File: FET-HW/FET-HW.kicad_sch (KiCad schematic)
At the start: 12 parts

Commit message: Remember that I needed 3x FETS per leg
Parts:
- removed N? (x2): Pad_4x2, N_NonPart:Pad_4x2, symbol N_NonPart:Pad_4x2
- removed Q? (x6): IRF7769L1TRPBF, Q_MOSFET:IR_DirectFET_L8, symbol Q_MOSFET:IRF7769L1TRPBF
- added N4, N5: Pad_4x2, N_NonPart:Pad_4x2, symbol N_NonPart:Pad_4x2
- gave numbers to parts that had none: 4
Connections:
- net PHASE_B: now also N4.1
- net PHASE_C: now also N5.1
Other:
- added sheet Half-Bridge-A (Half-Bridge.kicad_sch)
- added sheet Half-Bridge-B (Half-Bridge.kicad_sch)
- added sheet Half-Bridge-C (Half-Bridge.kicad_sch)
- note removed: "BLCD Interface"
- moved on the sheet: N3

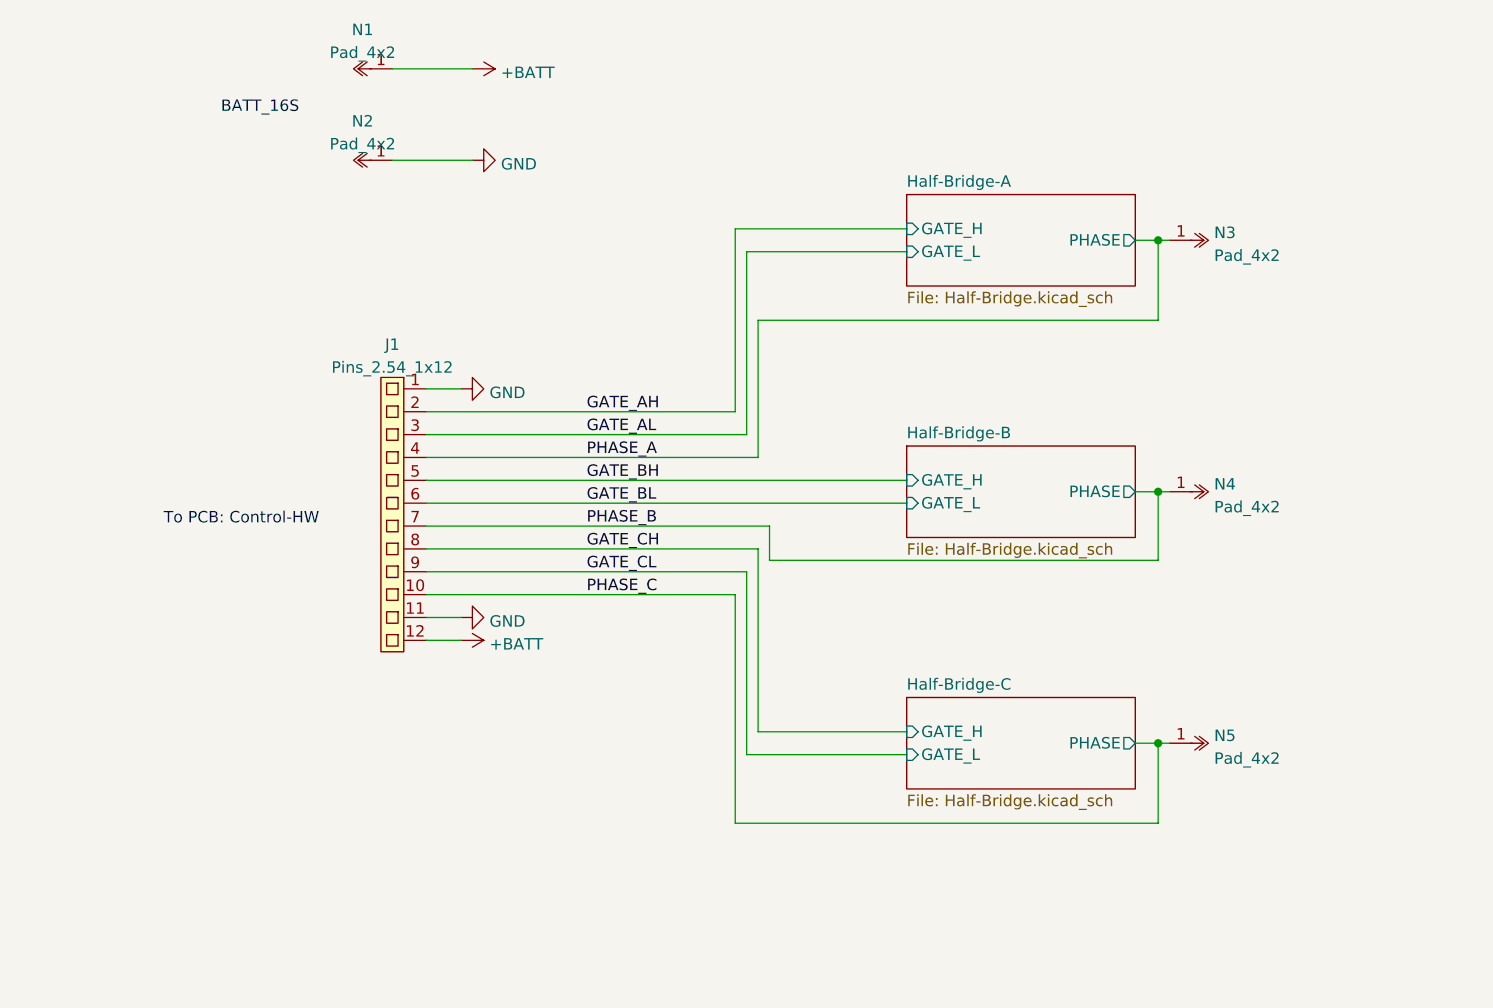
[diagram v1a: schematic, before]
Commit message: First pass at FET PCB layout
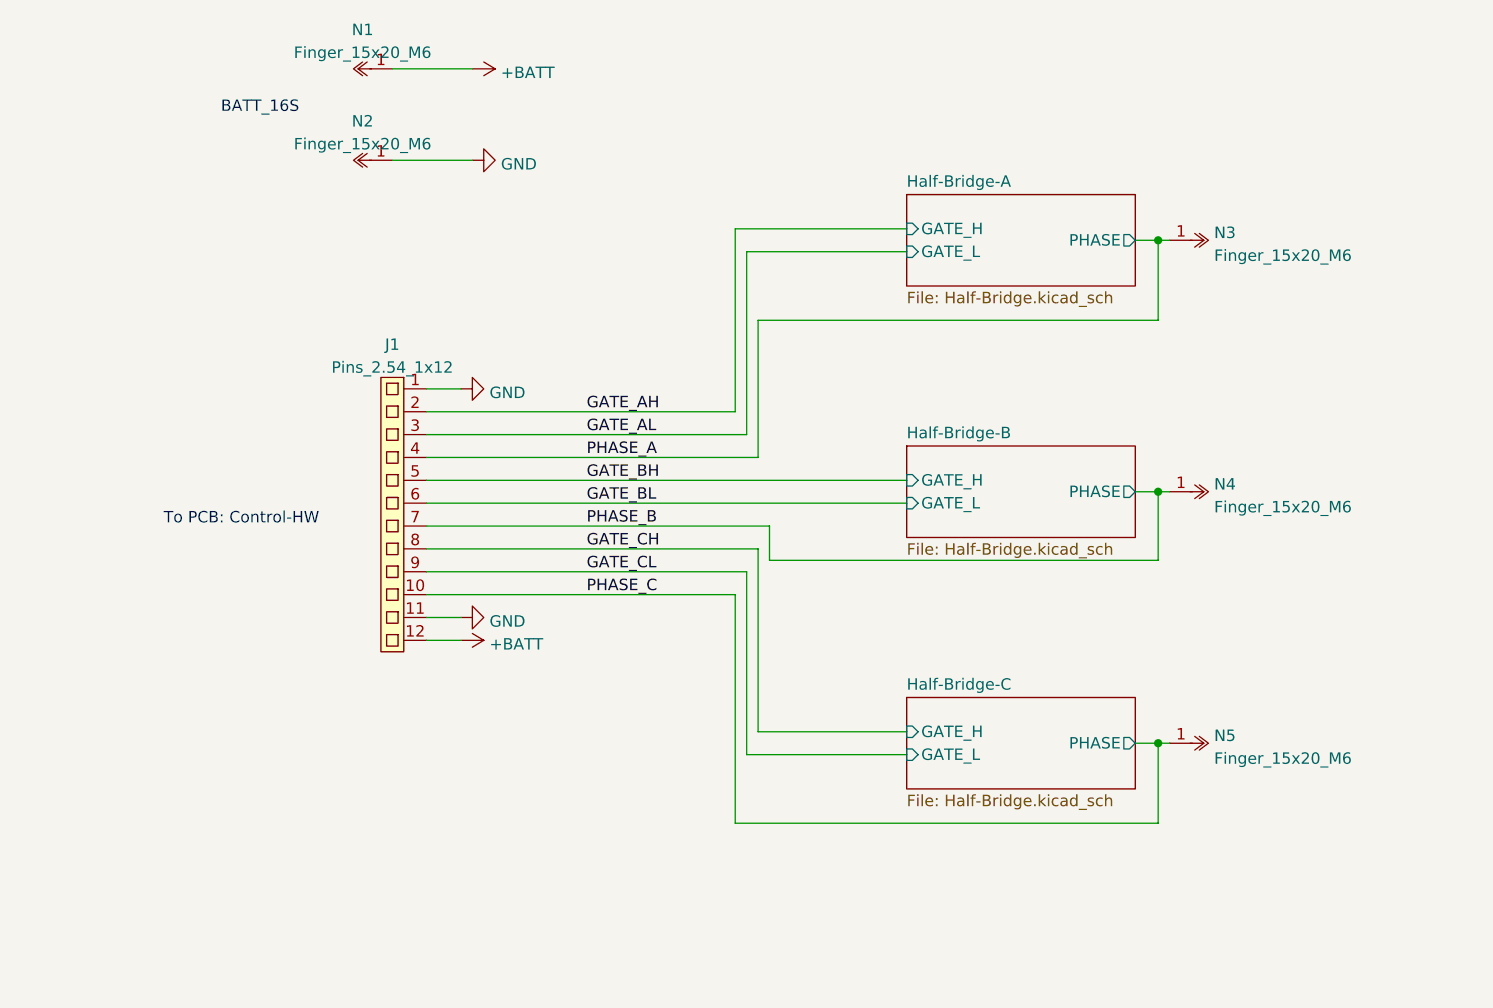
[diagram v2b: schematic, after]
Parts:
- removed N1, N2, N3, N4, N5: Pad_4x2, N_NonPart:Pad_4x2, symbol N_NonPart:Pad_4x2
- added N1, N2, N3, N4, N5: Finger_15x20_M6, N_NonPart:Finger_15x20_M6, symbol N_NonPart:Finger_15x20_M6
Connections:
- net +BATT: now also N1.1
- net GND: now also N2.1
- net PHASE_A: now also N3.1
- net PHASE_B: now also N4.1
- net PHASE_C: now also N5.1
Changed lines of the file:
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@@
     (pin "1")
   )
-  (symbol (lib_id "N_NonPart:Pad_4x2") (at 172.72 119.38 0) (unit 1)
+  (symbol (lib_id "N_NonPart:Finger_15x20_M6") (at 172.72 119.38 0) (unit 1)
     (in_bom no) (on_board yes) (fields_autoplaced)
     (property "Reference" "N5" (id 0) (at 176.403 118.5453 0)
       (effects (font (size 1.27 1.27)) (justify left))
     )
-    (property "Value" "Pad_4x2" (id 1) (at 176.403 121.0822 0)
-      (effects (font (size 1.27 1.27)) (justify left))
-    )
-    (property "Footprint" "N_NonPart:Pad_4x2" (id 2) (at 172.72 121.666 0)
+    (property "Value" "Finger_15x20_M6" (id 1) (at 176.403 121.0822 0)
+      (effects (font (size 1.27 1.27)) (justify left))
+    )
+    (property "Footprint" "N_NonPart:Finger_15x20_M6" (id 2) (at 172.72 121.666 0)
       (effects (font (size 1.27 1.27)) hide)
     )
     (property "Datasheet" "" (id 3) (at 172.72 121.666 0)
-      (effects (font (size 1.27 1.27)) hide)
-    )
-    (pin "1")
-  )
-  (symbol (lib_id "N_NonPart:Pad_4x2") (at 83.82 44.45 180) (unit 1)
-    (in_bom no) (on_board yes) (fields_autoplaced)
-    (property "Reference" "N1" (id 0) (at 81.788 40.1152 0))
-    (property "Value" "Pad_4x2" (id 1) (at 81.788 42.6521 0))
-    (property "Footprint" "N_NonPart:Pad_4x2" (id 2) (at 83.82 42.164 0)
-      (effects (font (size 1.27 1.27)) hide)
-    )
-    (property "Datasheet" "" (id 3) (at 83.82 42.164 0)
       (effects (font (size 1.27 1.27)) hide)
     )
@@
     (pin "9")
   )
-  (symbol (lib_id "N_NonPart:Pad_4x2") (at 172.72 91.44 0) (unit 1)
+  (symbol (lib_id "N_NonPart:Finger_15x20_M6") (at 172.72 91.44 0) (unit 1)
     (in_bom no) (on_board yes) (fields_autoplaced)
     (property "Reference" "N4" (id 0) (at 176.403 90.6053 0)
       (effects (font (size 1.27 1.27)) (justify left))
     )
-    (property "Value" "Pad_4x2" (id 1) (at 176.403 93.1422 0)
-      (effects (font (size 1.27 1.27)) (justify left))
-    )
-    (property "Footprint" "N_NonPart:Pad_4x2" (id 2) (at 172.72 93.726 0)
+    (property "Value" "Finger_15x20_M6" (id 1) (at 176.403 93.1422 0)
+      (effects (font (size 1.27 1.27)) (justify left))
+    )
+    (property "Footprint" "N_NonPart:Finger_15x20_M6" (id 2) (at 172.72 93.726 0)
       (effects (font (size 1.27 1.27)) hide)
     )
@@
     (pin "1")
   )
-  (symbol (lib_id "N_NonPart:Pad_4x2") (at 83.82 54.61 180) (unit 1)
+  (symbol (lib_id "N_NonPart:Finger_15x20_M6") (at 83.82 44.45 180) (unit 1)
+    (in_bom no) (on_board yes) (fields_autoplaced)
+    (property "Reference" "N1" (id 0) (at 81.788 40.1152 0))
+    (property "Value" "Finger_15x20_M6" (id 1) (at 81.788 42.6521 0))
+    (property "Footprint" "N_NonPart:Finger_15x20_M6" (id 2) (at 83.82 42.164 0)
+      (effects (font (size 1.27 1.27)) hide)
+    )
+    (property "Datasheet" "" (id 3) (at 83.82 42.164 0)
+      (effects (font (size 1.27 1.27)) hide)
+    )
+    (pin "1")
+  )
+  (symbol (lib_id "N_NonPart:Finger_15x20_M6") (at 172.72 63.5 0) (unit 1)
+    (in_bom no) (on_board yes) (fields_autoplaced)
+    (property "Reference" "N3" (id 0) (at 176.403 62.6653 0)
+      (effects (font (size 1.27 1.27)) (justify left))
+    )
+    (property "Value" "Finger_15x20_M6" (id 1) (at 176.403 65.2022 0)
+      (effects (font (size 1.27 1.27)) (justify left))
+    )
+    (property "Footprint" "N_NonPart:Finger_15x20_M6" (id 2) (at 172.72 65.786 0)
+      (effects (font (size 1.27 1.27)) hide)
+    )
+    (property "Datasheet" "" (id 3) (at 172.72 65.786 0)
+      (effects (font (size 1.27 1.27)) hide)
+    )
+    (pin "1")
+  )
+  (symbol (lib_id "power:GND") (at 93.98 54.61 90) (unit 1)
+    (in_bom yes) (on_board yes) (fields_autoplaced)
+    (property "Reference" "#PWR05" (id 0) (at 100.33 54.61 0)
+      (effects (font (size 1.27 1.27)) hide)
+    )
+    (property "Value" "GND" (id 1) (at 97.155 55.0438 90)
+      (effects (font (size 1.27 1.27)) (justify right))
+    )
+    (property "Footprint" "" (id 2) (at 93.98 54.61 0)
+      (effects (font (size 1.27 1.27)) hide)
+    )
+    (property "Datasheet" "" (id 3) (at 93.98 54.61 0)
+      (effects (font (size 1.27 1.27)) hide)
+    )
+    (pin "1")
+  )
+  (symbol (lib_id "N_NonPart:Finger_15x20_M6") (at 83.82 54.61 180) (unit 1)
     (in_bom no) (on_board yes) (fields_autoplaced)
     (property "Reference" "N2" (id 0) (at 81.788 50.2752 0))
-    (property "Value" "Pad_4x2" (id 1) (at 81.788 52.8121 0))
-    (property "Footprint" "N_NonPart:Pad_4x2" (id 2) (at 83.82 52.324 0)
+    (property "Value" "Finger_15x20_M6" (id 1) (at 81.788 52.8121 0))
+    (property "Footprint" "N_NonPart:Finger_15x20_M6" (id 2) (at 83.82 52.324 0)
       (effects (font (size 1.27 1.27)) hide)
     )
@@
     (pin "1")
   )
-  (symbol (lib_id "power:GND") (at 93.98 54.61 90) (unit 1)
-    (in_bom yes) (on_board yes) (fields_autoplaced)
-    (property "Reference" "#PWR05" (id 0) (at 100.33 54.61 0)
-      (effects (font (size 1.27 1.27)) hide)
-    )
-    (property "Value" "GND" (id 1) (at 97.155 55.0438 90)
-      (effects (font (size 1.27 1.27)) (justify right))
-    )
-    (property "Footprint" "" (id 2) (at 93.98 54.61 0)
-      (effects (font (size 1.27 1.27)) hide)
-    )
-    (property "Datasheet" "" (id 3) (at 93.98 54.61 0)
-      (effects (font (size 1.27 1.27)) hide)
-    )
-    (pin "1")
-  )
   (symbol (lib_id "power:GND") (at 92.71 80.01 90) (unit 1)
     (in_bom yes) (on_board yes) (fields_autoplaced)
@@
     )
     (property "Datasheet" "" (id 3) (at 92.71 80.01 0)
-      (effects (font (size 1.27 1.27)) hide)
-    )
-    (pin "1")
-  )
-  (symbol (lib_id "N_NonPart:Pad_4x2") (at 172.72 63.5 0) (unit 1)
-    (in_bom no) (on_board yes) (fields_autoplaced)
-    (property "Reference" "N3" (id 0) (at 176.403 62.6653 0)
-      (effects (font (size 1.27 1.27)) (justify left))
-    )
-    (property "Value" "Pad_4x2" (id 1) (at 176.403 65.2022 0)
-      (effects (font (size 1.27 1.27)) (justify left))
-    )
-    (property "Footprint" "N_NonPart:Pad_4x2" (id 2) (at 172.72 65.786 0)
-      (effects (font (size 1.27 1.27)) hide)
-    )
-    (property "Datasheet" "" (id 3) (at 172.72 65.786 0)
       (effects (font (size 1.27 1.27)) hide)
     )
@@
       (reference "J1") (unit 1) (value "Pins_2.54_1x12") (footprint "J_Connector:Pins-2.54-1x12")
     )
-    (path "/58fb4bc1-731e-4204-980e-6ae92e5db745"
-      (reference "N1") (unit 1) (value "Pad_4x2") (footprint "N_NonPart:Pad_4x2")
-    )
-    (path "/c0af76b2-c6cd-484b-9600-7264c4402718"
-      (reference "N2") (unit 1) (value "Pad_4x2") (footprint "N_NonPart:Pad_4x2")
-    )
-    (path "/fd8f2510-b7d0-403f-b72c-331695ad847e"
-      (reference "N3") (unit 1) (value "Pad_4x2") (footprint "N_NonPart:Pad_4x2")
-    )
-    (path "/93c45f36-289f-4e81-aacd-b0a0b48c976e"
-      (reference "N4") (unit 1) (value "Pad_4x2") (footprint "N_NonPart:Pad_4x2")
-    )
-    (path "/47ecc25e-d63d-4fbf-83a0-da94dbfca2e1"
-      (reference "N5") (unit 1) (value "Pad_4x2") (footprint "N_NonPart:Pad_4x2")
+    (path "/bc168ec1-0ec6-47fd-8f30-f55b54966470"
+      (reference "N1") (unit 1) (value "Finger_15x20_M6") (footprint "N_NonPart:Finger_15x20_M6")
+    )
+    (path "/f66bdee5-96a9-40a8-b12b-f47f093caa78"
+      (reference "N2") (unit 1) (value "Finger_15x20_M6") (footprint "N_NonPart:Finger_15x20_M6")
+    )
+    (path "/d5bc994d-8168-43db-aa02-7165c6cdcf97"
+      (reference "N3") (unit 1) (value "Finger_15x20_M6") (footprint "N_NonPart:Finger_15x20_M6")
+    )
+    (path "/927a2a28-5ab0-4dab-ac00-74d0025982a9"
+      (reference "N4") (unit 1) (value "Finger_15x20_M6") (footprint "N_NonPart:Finger_15x20_M6")
+    )
+    (path "/07a1227f-3215-4c86-b43d-c35adb180294"
+      (reference "N5") (unit 1) (value "Finger_15x20_M6") (footprint "N_NonPart:Finger_15x20_M6")
     )
     (path "/72a3fdbf-6925-4f35-b34d-606e2de19b01/49f7de4b-9c2c-456c-b3f9-748cf3ce6f34"

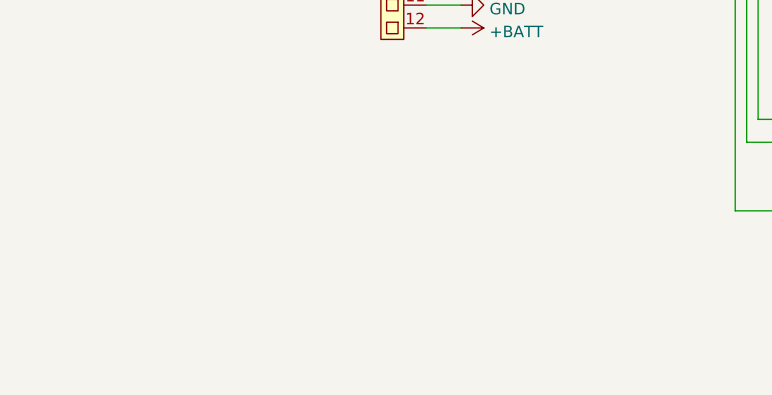
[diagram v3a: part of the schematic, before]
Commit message: Add TH capacitors
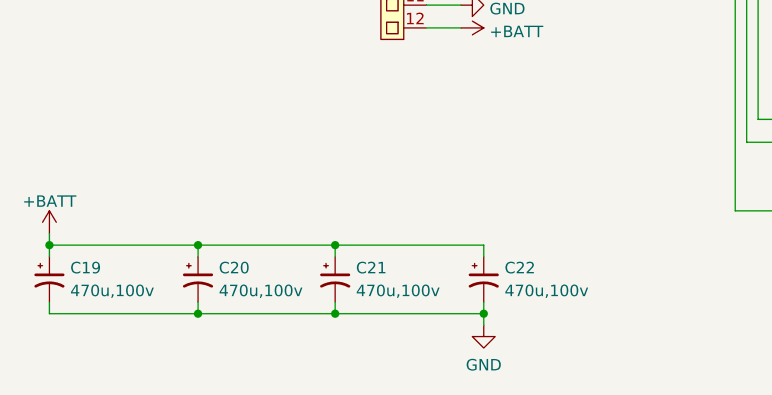
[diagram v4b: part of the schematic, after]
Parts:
- added C19, C20, C21, C22: 470u,100v, Capacitor_THT:C_Radial_D16.0mm_H25.0mm_P7.50mm, symbol Device:C_Polarized_Small_US
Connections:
- net +BATT: now also C19.1, C20.1, C21.1, C22.1
- net GND: now also C19.2, C20.2, C21.2, C22.2
